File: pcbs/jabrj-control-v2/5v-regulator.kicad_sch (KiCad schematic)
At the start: 47 parts, among them Q401 DMN21D2UFB-7B, Q402 DMN21D2UFB-7B, Q403 DMN21D2UFB-7B, U401 AZV3001FZ4-7, U402 TPS259472ARPWR, U403 MAX20008AFOC/VY+T

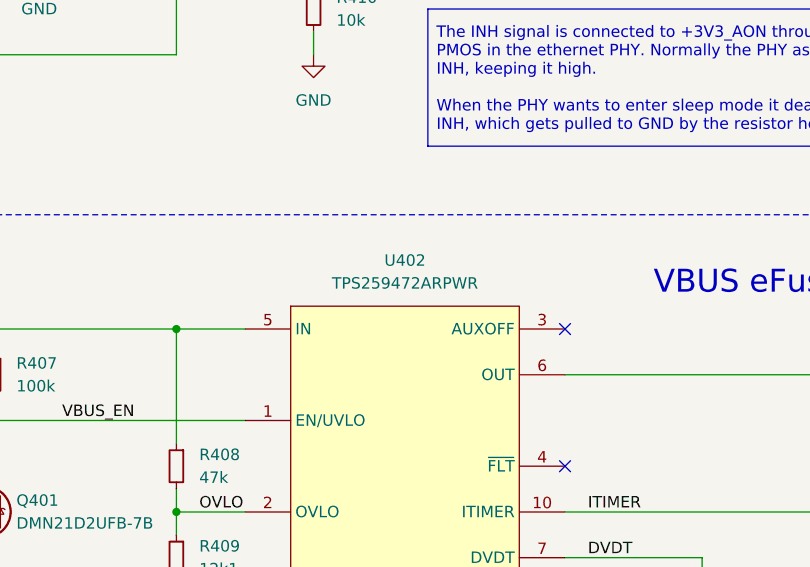
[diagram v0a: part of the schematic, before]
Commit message: Updated all line endings
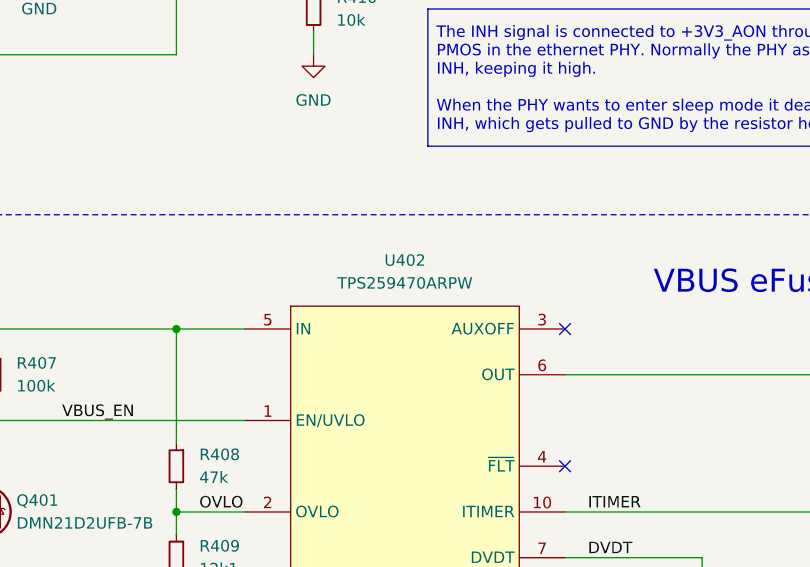
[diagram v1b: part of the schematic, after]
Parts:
- U402: value TPS259472ARPWR -> TPS259470ARPW
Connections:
- net DVDT: no longer U402.14 (DVDT)
- net ITIMER: no longer U402.11 (ITIMER)
- net VBUS_EN: no longer U402.12 (EN/UVLO)
- net at U402.4 (~{FLT}): no longer U402.13 (~{FLT})
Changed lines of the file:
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@@
 			)
 		)
-		(property "Value" "TPS259472ARPWR"
+		(property "Value" "TPS259470ARPW"
 			(at 114.3 129.54 0)
 			(show_name no)
@@
 			)
 		)
-		(property "Field6" ""
-			(at 114.3 132.08 0)
-			(hide yes)
-			(show_name no)
-			(do_not_autoplace no)
-			(effects
-				(font
-					(size 1.27 1.27)
-				)
-			)
-		)
-		(property "Field7" ""
-			(at 114.3 132.08 0)
-			(hide yes)
-			(show_name no)
-			(do_not_autoplace no)
-			(effects
-				(font
-					(size 1.27 1.27)
-				)
-			)
-		)
-		(property "Part Description" ""
-			(at 114.3 132.08 0)
-			(hide yes)
-			(show_name no)
-			(do_not_autoplace no)
-			(effects
-				(font
-					(size 1.27 1.27)
-				)
-			)
-		)
-		(property "Critical Parameter" ""
-			(at 114.3 132.08 0)
-			(hide yes)
-			(show_name no)
-			(do_not_autoplace no)
-			(effects
-				(font
-					(size 1.27 1.27)
-				)
-			)
-		)
-		(property "IRP,40K (A)" ""
-			(at 114.3 132.08 0)
-			(hide yes)
-			(show_name no)
-			(do_not_autoplace no)
-			(effects
-				(font
-					(size 1.27 1.27)
-				)
-			)
-		)
-		(property "ISAT,10% (A)" ""
-			(at 114.3 132.08 0)
-			(hide yes)
-			(show_name no)
-			(do_not_autoplace no)
-			(effects
-				(font
-					(size 1.27 1.27)
-				)
-			)
-		)
-		(property "ISAT,30% (A)" ""
-			(at 114.3 132.08 0)
-			(hide yes)
-			(show_name no)
-			(do_not_autoplace no)
-			(effects
-				(font
-					(size 1.27 1.27)
-				)
-			)
-		)
-		(property "L (µH)" ""
-			(at 114.3 132.08 0)
-			(hide yes)
-			(show_name no)
-			(do_not_autoplace no)
-			(effects
-				(font
-					(size 1.27 1.27)
-				)
-			)
-		)
-		(property "Manufacturer" ""
-			(at 114.3 132.08 0)
-			(hide yes)
-			(show_name no)
-			(do_not_autoplace no)
-			(effects
-				(font
-					(size 1.27 1.27)
-				)
-			)
-		)
-		(property "Manufacturer URL" ""
-			(at 114.3 132.08 0)
-			(hide yes)
-			(show_name no)
-			(do_not_autoplace no)
-			(effects
-				(font
-					(size 1.27 1.27)
-				)
-			)
-		)
-		(property "Match Code" ""
-			(at 114.3 132.08 0)
-			(hide yes)
-			(show_name no)
-			(do_not_autoplace no)
-			(effects
-				(font
-					(size 1.27 1.27)
-				)
-			)
-		)
-		(property "Mounting Technology" ""
-			(at 114.3 132.08 0)
-			(hide yes)
-			(show_name no)
-			(do_not_autoplace no)
-			(effects
-				(font
-					(size 1.27 1.27)
-				)
-			)
-		)
-		(property "Part Number" ""
-			(at 114.3 132.08 0)
-			(hide yes)
-			(show_name no)
-			(do_not_autoplace no)
-			(effects
-				(font
-					(size 1.27 1.27)
-				)
-			)
-		)
-		(property "Published Date" ""
-			(at 114.3 132.08 0)
-			(hide yes)
-			(show_name no)
-			(do_not_autoplace no)
-			(effects
-				(font
-					(size 1.27 1.27)
-				)
-			)
-		)
-		(property "RDC max. (mΩ)" ""
-			(at 114.3 132.08 0)
-			(hide yes)
-			(show_name no)
-			(do_not_autoplace no)
-			(effects
-				(font
-					(size 1.27 1.27)
-				)
-			)
-		)
-		(property "RDC typ. (mΩ)" ""
-			(at 114.3 132.08 0)
-			(hide yes)
-			(show_name no)
-			(do_not_autoplace no)
-			(effects
-				(font
-					(size 1.27 1.27)
-				)
-			)
-		)
-		(property "Size" ""
-			(at 114.3 132.08 0)
-			(hide yes)
-			(show_name no)
-			(do_not_autoplace no)
-			(effects
-				(font
-					(size 1.27 1.27)
-				)
-			)
-		)
-		(property "Type/Size" ""
-			(at 114.3 132.08 0)
-			(hide yes)
-			(show_name no)
-			(do_not_autoplace no)
-			(effects
-				(font
-					(size 1.27 1.27)
-				)
-			)
-		)
-		(property "VOP (V)" ""
-			(at 114.3 132.08 0)
-			(hide yes)
-			(show_name no)
-			(do_not_autoplace no)
-			(effects
-				(font
-					(size 1.27 1.27)
-				)
-			)
-		)
-		(property "fres (MHz)" ""
-			(at 114.3 132.08 0)
-			(hide yes)
-			(show_name no)
-			(do_not_autoplace no)
-			(effects
-				(font
-					(size 1.27 1.27)
-				)
-			)
-		)
 		(pin "2"
 		)
@@
 		(pin "1"
 		)
-		(pin "12"
-		)
-		(pin "13"
-		)
 		(pin "8"
 		)
@@
 		(pin "7"
 		)
-		(pin "14"
-		)
 		(pin "9"
 		)
-		(pin "11"
-		)
 		(instances

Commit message: DRC Clean
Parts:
- added TP403: 1.5mm, project_footprints:TestPoint_Pad_D1.5mm, symbol Connector:TestPoint_Small
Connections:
- net VBUS: now also TP403.1
